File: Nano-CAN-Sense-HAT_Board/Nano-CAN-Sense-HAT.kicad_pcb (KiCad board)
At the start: 2 copper layers, 45.7 x 20.3 mm, 37 parts, among them J1 Analog, J2 Digital, J3 Conn_02x04_Counter_Clockwise, J4 Conn_02x04_Counter_Clockwise, J5 Conn_01x05, J6 Conn_01x03, SW1 SW_Push, SW2 SW_Push, U1 LMC6484, U4 TCAN1044A

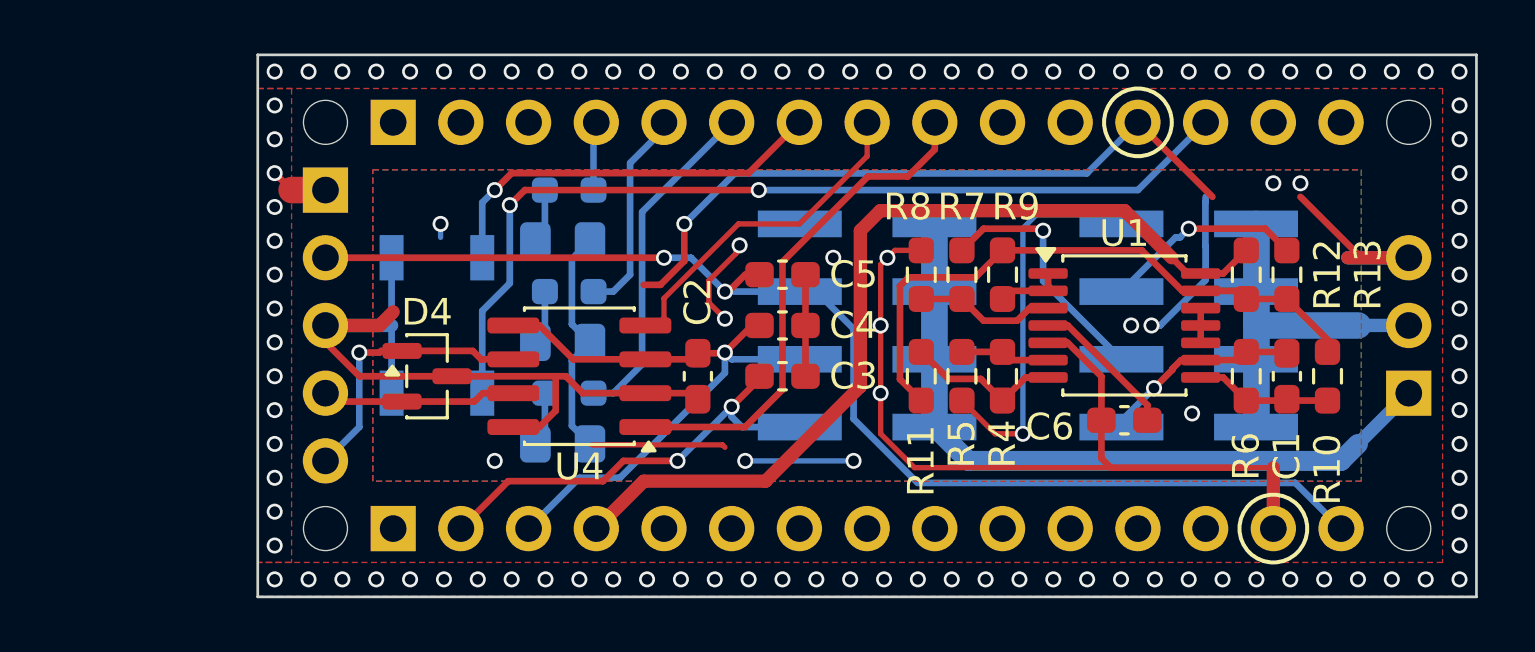
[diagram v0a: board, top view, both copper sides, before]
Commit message: Improved Can for CAN-FD
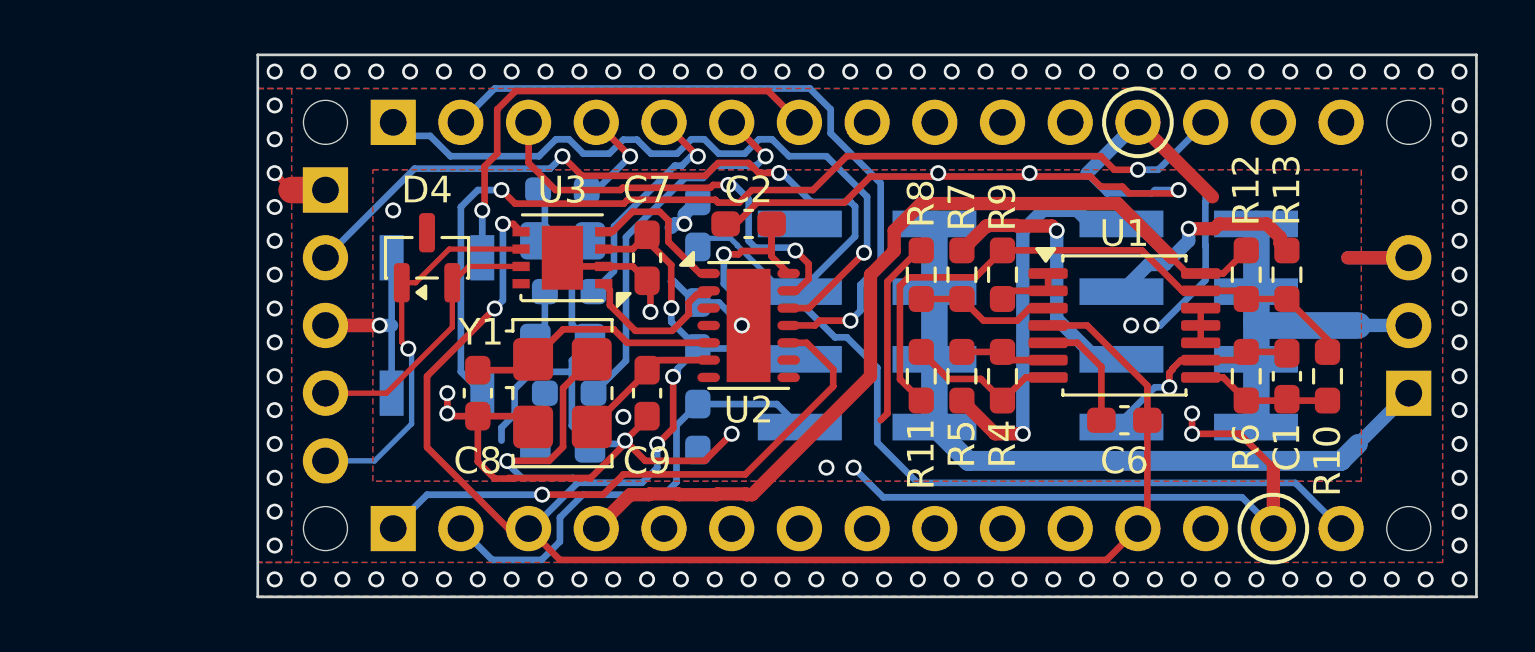
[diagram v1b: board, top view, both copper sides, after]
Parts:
- removed U4: TCAN1044A, Package_SO:SOIC-8_3.9x4.9mm_P1.27mm
- added C7: 100nC, Capacitor_SMD:C_0603_1608Metric_Pad1.08x0.95mm_HandSolder, F.Cu at (113.3, 88.6)
- added C8: 22pC, Capacitor_SMD:C_0603_1608Metric_Pad1.08x0.95mm_HandSolder, F.Cu at (107.0, 93.7)
- added C9: 22pC, Capacitor_SMD:C_0603_1608Metric_Pad1.08x0.95mm_HandSolder, F.Cu at (113.3, 93.7)
- added U2: MCP2518FD-xQBB, Package_DFN_QFN:DFN-14-1EP_3x4.5mm_P0.65mm_EP1.65x4.25mm, F.Cu at (117.1, 91.1)
- added U3: MCP2542FDxMF, Package_DFN_QFN:DFN-8-1EP_3x3mm_P0.65mm_EP1.55x2.4mm, F.Cu at (110.2, 88.6)
- added Y1: SG-5032CCN, Oscillator:Oscillator_SMD_SeikoEpson_SG8002LB-4Pin_5.0x3.2mm, F.Cu at (110.2, 93.7)
- C3, C4, C5: moved to B.Cu
- moved C2 6.02 mm to (117.1, 87.3), turned to 0 degrees
- moved D4 4.45 mm to (105.1, 88.6), turned to 90 degrees
- moved C3 3.70 mm to (115.2, 94.9), turned to -90 degrees
- moved C5 3.70 mm to (115.2, 87.3), turned to 90 degrees
- moved C4 3.18 mm to (115.2, 91.1), turned to 90 degrees
- moved R3 0.25 mm to (110.2, 86.0)
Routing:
- net +5V: track 28.7 -> 88.5 mm, vias 1 -> 7
- net /*D11/MOSI: track 0.00 -> 26.3 mm, vias 0 -> 1
- net /D12/MISO: track 0.00 -> 25.9 mm, vias 0 -> 1
- net /D13/SCK: track 0.00 -> 21.4 mm, vias 0 -> 1
- net /D4: track 19.0 -> 0.00 mm
- net /*D10/SS: track 0.00 -> 16.2 mm, vias 0 -> 2
- net /*D5: track 13.2 -> 0.00 mm
- net VCC: track 45.2 -> 56.3 mm
- net /SPXOin: track 0.00 -> 9.50 mm
- net Net-(U2-RXCAN): track 0.00 -> 5.97 mm
- net GND: track 131.3 -> 125.5 mm, vias 16 -> 19
- net Net-(U2-TXCAN): track 0.00 -> 5.68 mm
- net /SPXOout: track 0.00 -> 5.42 mm
- net /CAN_LO: track 10.5 -> 14.3 mm
- net /CAN_HI: track 6.87 -> 10.3 mm
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- added copper zone on B.Cu, net Earth_Shield
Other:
- board text added: "12V"
- board text added: "20mA"
- board text added: "3.3V"
- board text added: "5V"
- board text added: "OUT"
- board text added: "Sense"

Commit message: Added images, and Readme
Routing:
- net GND: track 125.5 -> 124.8 mm, vias 19 -> 18

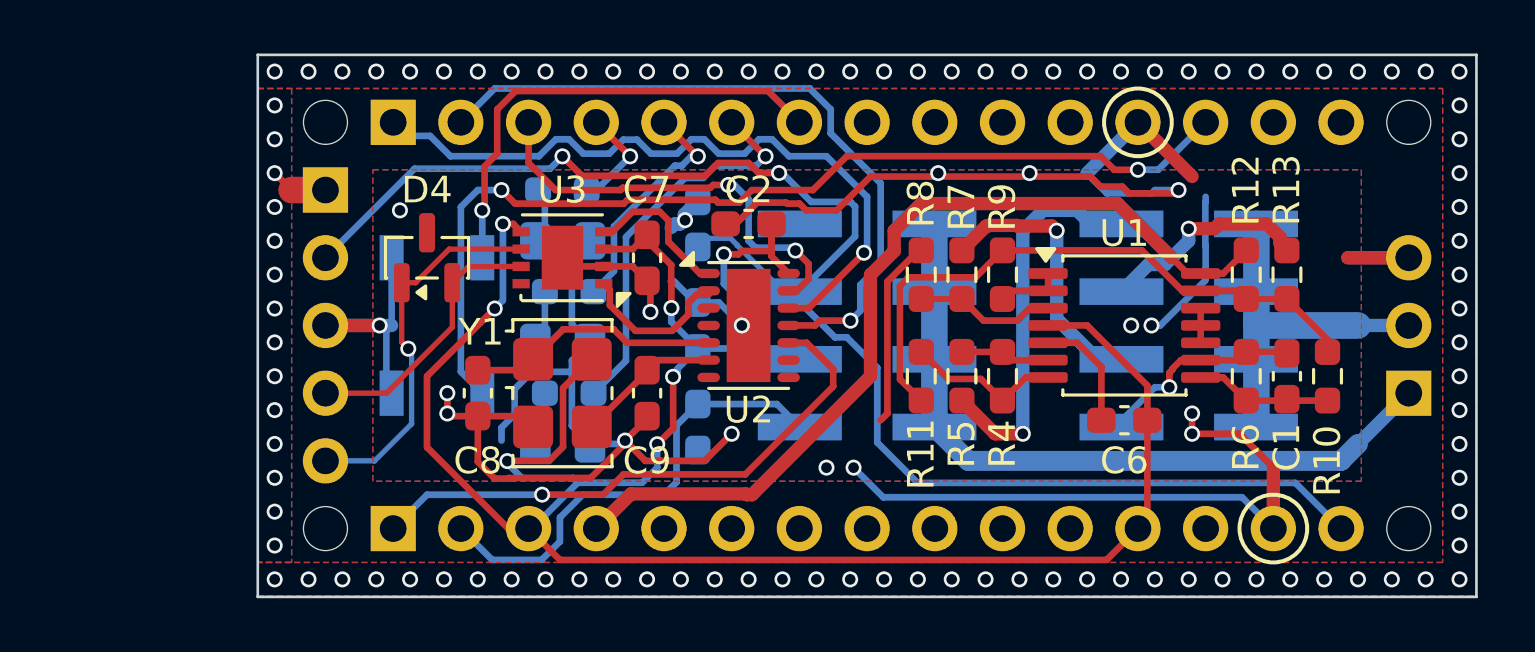
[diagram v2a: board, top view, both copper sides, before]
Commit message: Added Temp sensor SHT4x, rounded board edge
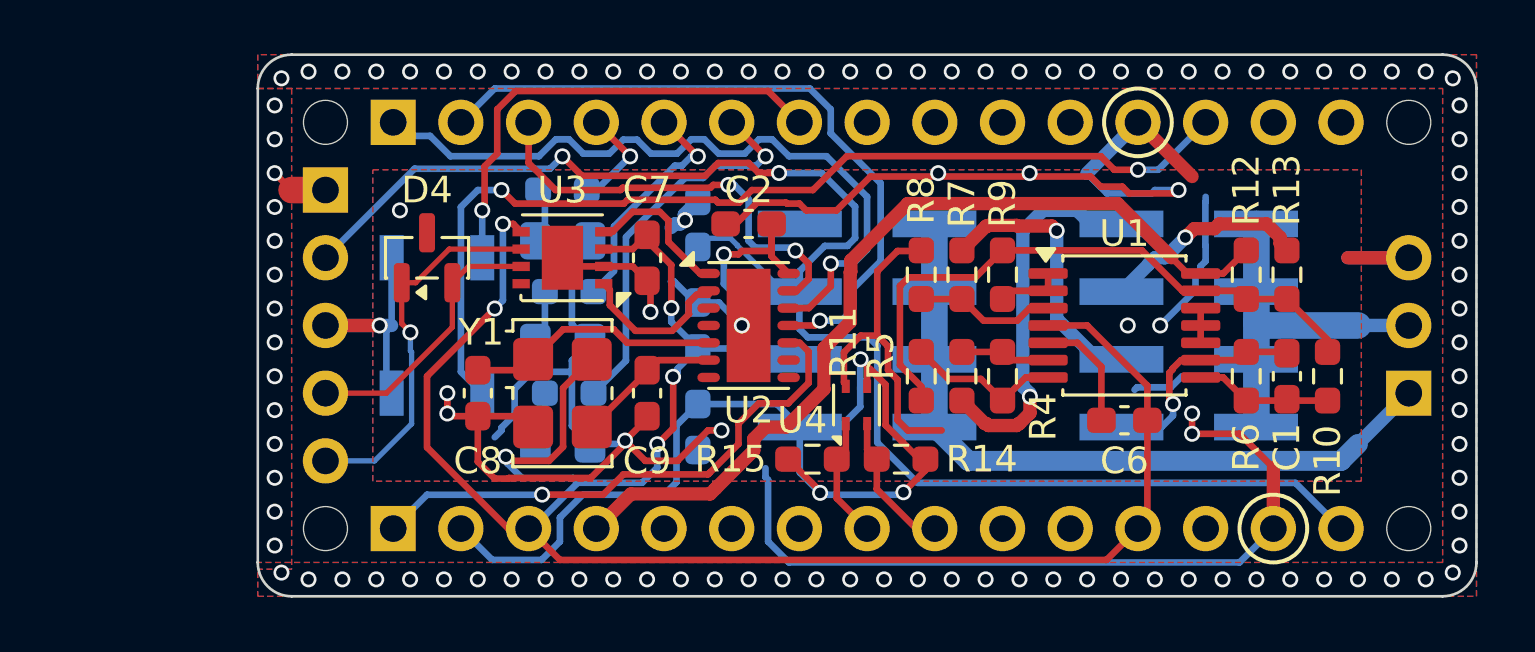
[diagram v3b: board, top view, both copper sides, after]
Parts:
- added R14: 1kR, Resistor_SMD:R_0603_1608Metric_Pad0.98x0.95mm_HandSolder, F.Cu at (122.9, 96.1)
- added R15: 1kR, Resistor_SMD:R_0603_1608Metric_Pad0.98x0.95mm_HandSolder, F.Cu at (119.5, 96.1)
- added U4: SHT4x, Sensor_Humidity:Sensirion_DFN-4_1.5x1.5mm_P0.8mm_SHT4x_NoCentralPad, F.Cu at (121.2, 94.1)
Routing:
- net +3V3: track 17.8 -> 37.4 mm, vias 0 -> 3
- net GND: track 124.8 -> 137.5 mm, vias 18 -> 16
- net /A5/SCL: track 0.00 -> 5.40 mm
- net /A4/SDA: track 0.00 -> 4.55 mm
- net VCC: track 56.3 -> 57.8 mm
- net /sense_Current: track 7.13 -> 8.28 mm
- net /D13/SCK: track 21.4 -> 20.4 mm
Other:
- outline, holes or cut-outs redrawn

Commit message: Changed oscillator, improved GND layout
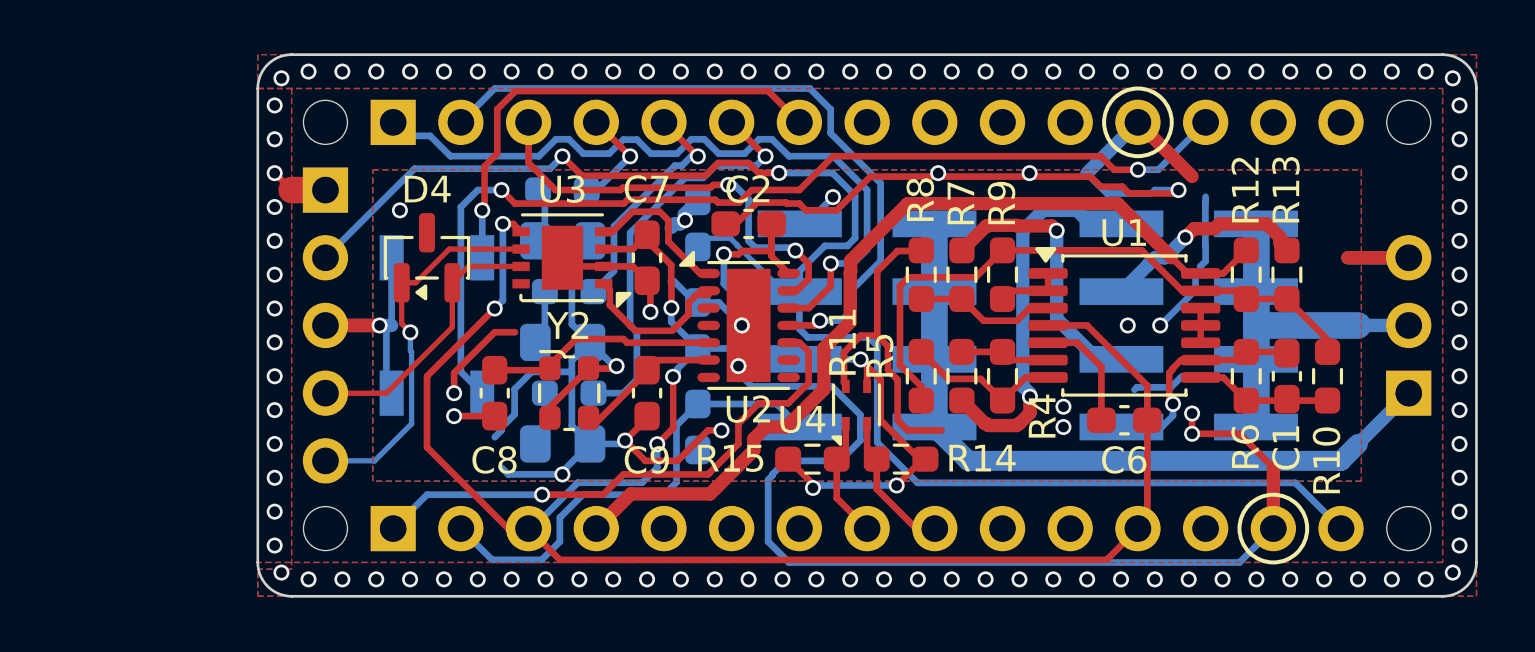
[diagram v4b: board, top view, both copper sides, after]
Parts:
- removed Y1: SG-5032CCN, Oscillator:Oscillator_SMD_SeikoEpson_SG8002LB-4Pin_5.0x3.2mm
- added Y2: ECS-200-8-33, Oscillator:Oscillator_SMD_ECS_2520MV-xxx-xx-4Pin_2.5x2.0mm, F.Cu at (110.4, 93.7)
- C8, C9: value 22pC -> 8pC
- moved C8 0.64 mm to (107.6, 93.7)
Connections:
- J3 pad 7: unconnected-(J3-Pin_7-Pad7) -> GND
- R14 pad 2: +3V3 -> +5V
- R15 pad 2: +3V3 -> +5V
- U4 pad 3: +3V3 -> +5V
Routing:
- net +3V3: track 37.4 -> 17.8 mm, vias 3 -> 0
- net GND: track 137.5 -> 151.5 mm, vias 16 -> 22
- net +5V: track 88.9 -> 93.8 mm, vias 7 -> 9
- net /D7: track 14.6 -> 15.5 mm
- net /SPXOin: track 9.50 -> 8.64 mm
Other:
- board text added: "GND"

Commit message: Added BOM, defined footprints
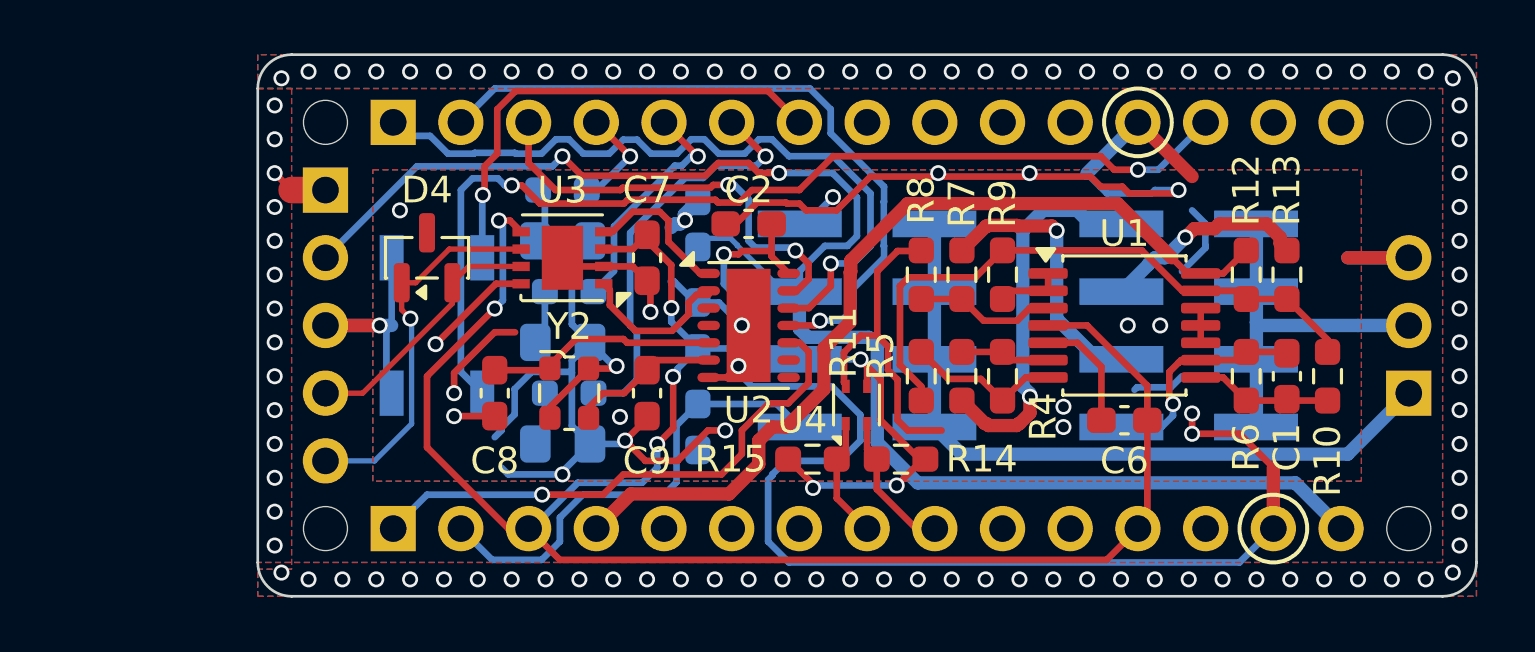
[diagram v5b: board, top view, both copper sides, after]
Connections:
- U3 pad 8: unconnected-(U3-STBY-Pad8) -> GND
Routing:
- net GND: track 151.5 -> 156.1 mm, vias 22 -> 24
- net /~{RESET}: track 37.5 -> 38.2 mm
- net +5V: track 93.8 -> 93.2 mm
- net /CAN_HI: track 10.3 -> 9.77 mm

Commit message: Rodone all rounting, changed to 4-layer baord
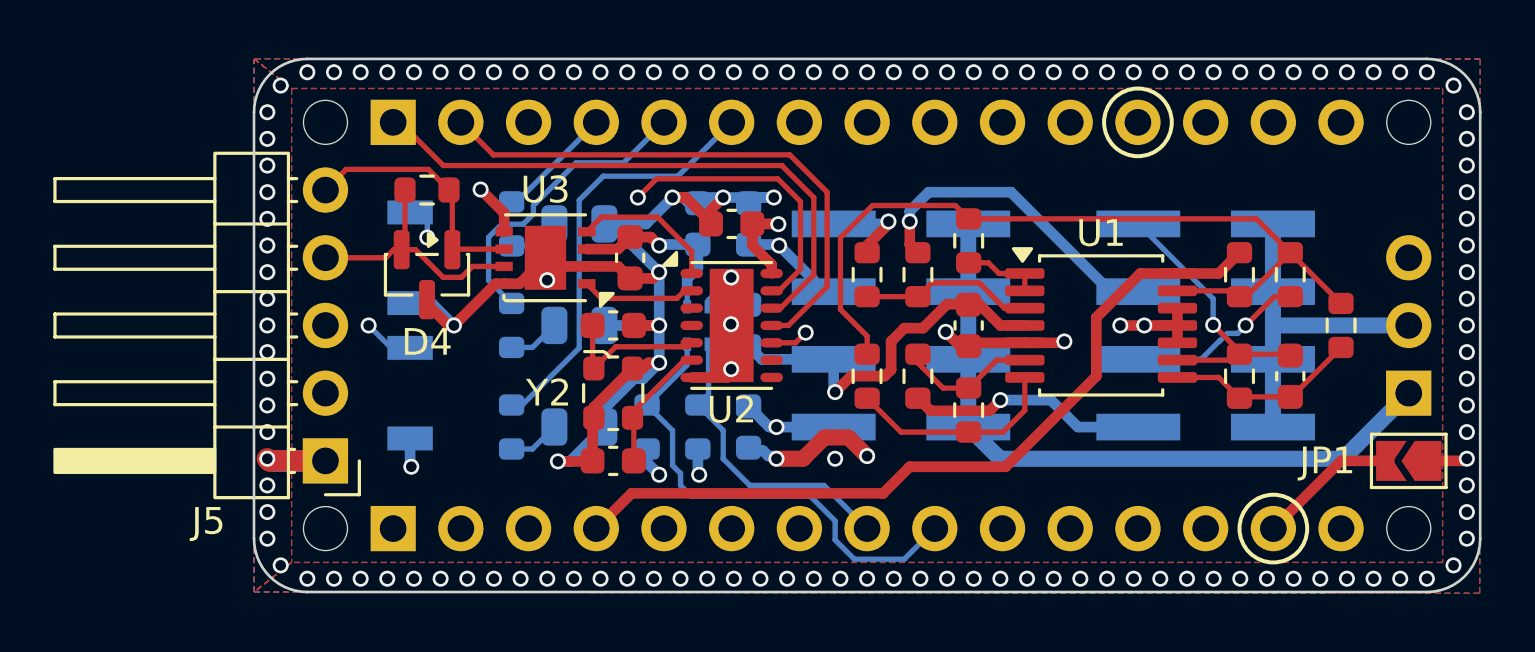
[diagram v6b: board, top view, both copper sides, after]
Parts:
- added C10: 100nC, Capacitor_SMD:C_0603_1608Metric, B.Cu at (115.2, 87.3)
- added JP1: SolderJumper_2_Open, Jumper:SolderJumper-2_P1.3mm_Open_TrianglePad1.0x1.5mm, F.Cu at (141.9, 96.2)
- added R16: 120R, Resistor_SMD:R_0603_1608Metric, F.Cu at (105.1, 86.0)
- C1, C2, C3, C4, C5, C6, C7, C8, C9: footprint Capacitor_SMD:C_0603_1608Metric_Pad1.08x0.95mm_HandSolder -> Capacitor_SMD:C_0603_1608Metric
- D1, D2, D3: footprint LED_SMD:LED_0805_2012Metric_Pad1.15x1.40mm_HandSolder -> LED_SMD:LED_0805_2012Metric
- J5: moved to F.Cu
- R1, R10, R11, R12, R13, R2, R3, R4, R5, R6, R7, R8, R9: footprint Resistor_SMD:R_0603_1608Metric_Pad0.98x0.95mm_HandSolder -> Resistor_SMD:R_0603_1608Metric
- R14, R15: footprint Resistor_SMD:R_0603_1608Metric_Pad0.98x0.95mm_HandSolder -> Resistor_SMD:R_0603_1608Metric; moved to B.Cu
- U4: moved to B.Cu
- moved J5 10.2 mm to (101.3, 96.2)
- moved R14 9.61 mm to (113.3, 94.9), turned to -90 degrees
- moved C6 6.84 mm to (125.4, 91.1), turned to -90 degrees
- moved U4 6.66 mm to (115.2, 91.1)
- moved C8 5.12 mm to (112.1, 91.1), turned to 180 degrees
- moved R15 4.46 mm to (115.2, 94.9), turned to -90 degrees
- moved C9 2.84 mm to (112.1, 96.2), turned to 0 degrees
- moved R1 2.50 mm to (108.3, 94.9), turned to -90 degrees
- moved R2 2.50 mm to (108.3, 91.1), turned to -90 degrees
- moved R3 2.29 mm to (108.3, 87.3), turned to -90 degrees
- moved R11 2.03 mm to (121.6, 93.0), turned to -90 degrees
- moved R8 2.03 mm to (121.6, 89.2)
- moved R10 1.97 mm to (139.4, 91.1)
- moved C3 1.91 mm to (117.1, 94.9)
- moved C4 1.91 mm to (117.1, 91.1)
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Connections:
- J4 pad 1: /Sense -> /sense3.3V
- J4 pad 2: /sense3.3V -> /Sense
- J4 pad 3: /Sense -> /sense5V
- J4 pad 4: /sense5V -> /Sense
- J4 pad 5: /Sense -> /sense12V
- J4 pad 6: /sense12V -> /Sense
- J4 pad 7: /Sense -> /sense_Current
- J4 pad 8: /sense_Current -> /Sense
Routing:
- net GND: track 156.1 -> 75.0 mm, vias 24 -> 20
- net +5V: track 93.2 -> 75.7 mm, vias 9 -> 7
- net /A5/SCL: track 5.40 -> 18.0 mm
- net VCC: track 58.1 -> 49.8 mm, vias 2 -> 1
- net Net-(U1D--): track 22.6 -> 30.6 mm
- net /A4/SDA: track 4.55 -> 11.3 mm
- net /sense3.3V: track 14.3 -> 9.05 mm
- net /*D11/MOSI: track 26.2 -> 21.1 mm, vias 1 -> 0
- net /CAN_LO: track 14.3 -> 9.52 mm, vias 1 -> 0
- net /D12/MISO: track 26.6 -> 21.9 mm, vias 1 -> 0
- net /A0: track 33.1 -> 29.7 mm
- net Earth_Shield: track 2.17 -> 5.54 mm, vias 100 -> 124
- net /SPXOin: track 8.64 -> 5.71 mm
- net /sense12V: track 9.48 -> 12.1 mm
- net /D8: track 8.79 -> 11.4 mm, vias 1 -> 0
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- added copper zone on In1.Cu, net Earth_Shield
- added copper zone on In2.Cu, net Earth_Shield
- added copper zone on In1.Cu, net GND
- removed copper zone on B.Cu, net GND
- removed copper zone on F.Cu, net GND
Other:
- board size 45.7 x 20.3 mm -> 46 x 20 mm
- copper layers 2 -> 4
- board text added: "ERR"
- board text added: "RESET"
- board text added: "RX"
- board text added: "TX"
- board text added: "USER"

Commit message: Minor board changes, cosmetics, new pictures
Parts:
- JP1: moved to B.Cu
- moved D4 0.64 mm to (105.1, 89.8)
- moved R16 0.64 mm to (105.1, 86.7)
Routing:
- net GND: track 75.0 -> 82.7 mm
- net +5V: track 75.7 -> 80.3 mm, vias 7 -> 8
- net /~{RESET}: track 37.7 -> 38.7 mm
- net /CAN_HI: track 9.72 -> 10.7 mm
- net /D13/SCK: track 22.8 -> 23.7 mm
- net /sense_Current: track 10.1 -> 10.8 mm
- net /*D6: track 18.5 -> 19.1 mm
